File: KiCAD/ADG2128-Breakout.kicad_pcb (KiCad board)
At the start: 2 copper layers, 18.8 x 36.6 mm, 10 parts, among them J1 Conn_01x14_Male, J2 Conn_01x14_Male, J3 Conn_01x03_Male, J4 Conn_01x03_Male, J5 Conn_01x03_Male, U1 ADG2128

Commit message: Fixing silk mistake.
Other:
- board text added: "Vcc GND SDA SCL ~RESET GND Y0 Y1 Y2 Y3 Y4 Y5 Y6 Y7"
- board text removed: "Vcc GND SDA SCL ~RESET SDA Y0 Y1 Y2 Y3 Y4 Y5 Y6 Y7"
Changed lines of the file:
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@@
     (effects (font (size 1.5 1.5) (thickness 0.3)) (justify left mirror))
   )
-  (gr_text "Vcc\nGND\nSDA\nSCL\n~RESET\nSDA\nY0\nY1\nY2\nY3\nY4\nY5\nY6\nY7" (at 24.5745 34.417) (layer B.SilkS)
+  (gr_text "Vcc\nGND\nSDA\nSCL\n~RESET\nGND\nY0\nY1\nY2\nY3\nY4\nY5\nY6\nY7" (at 24.5745 34.417) (layer B.SilkS)
     (effects (font (size 1.5 1.5) (thickness 0.3)) (justify right mirror))
   )

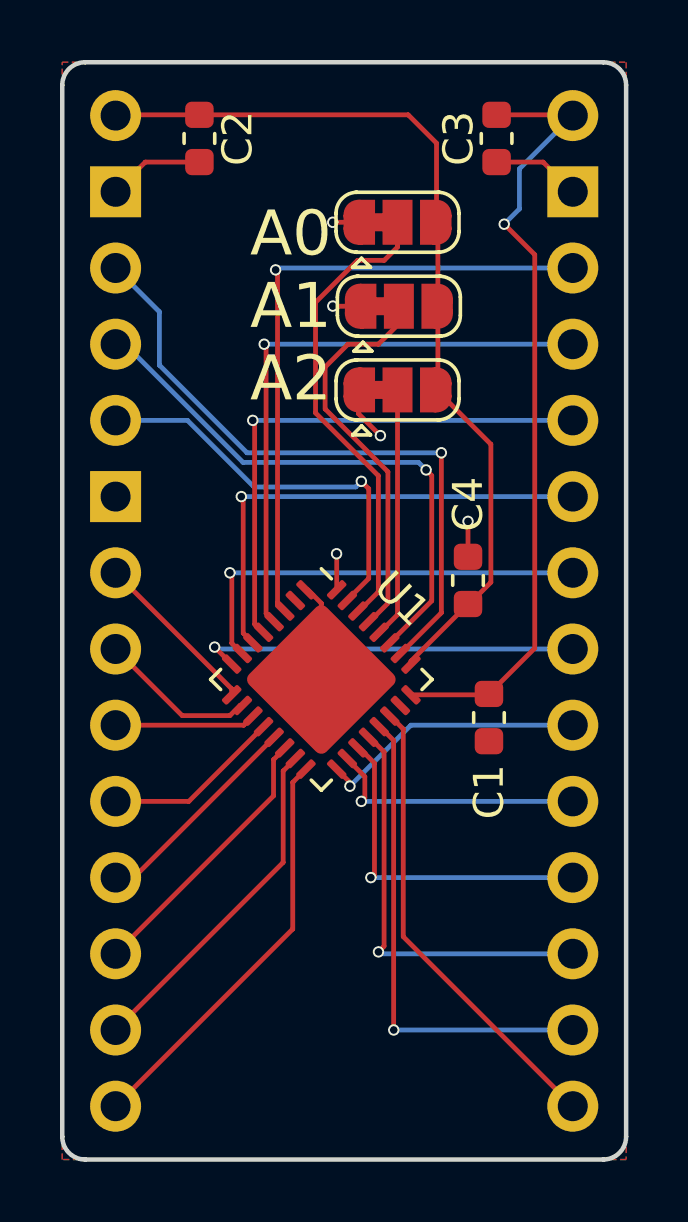
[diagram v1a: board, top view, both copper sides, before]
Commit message: Minor revisions for better manufacturability.
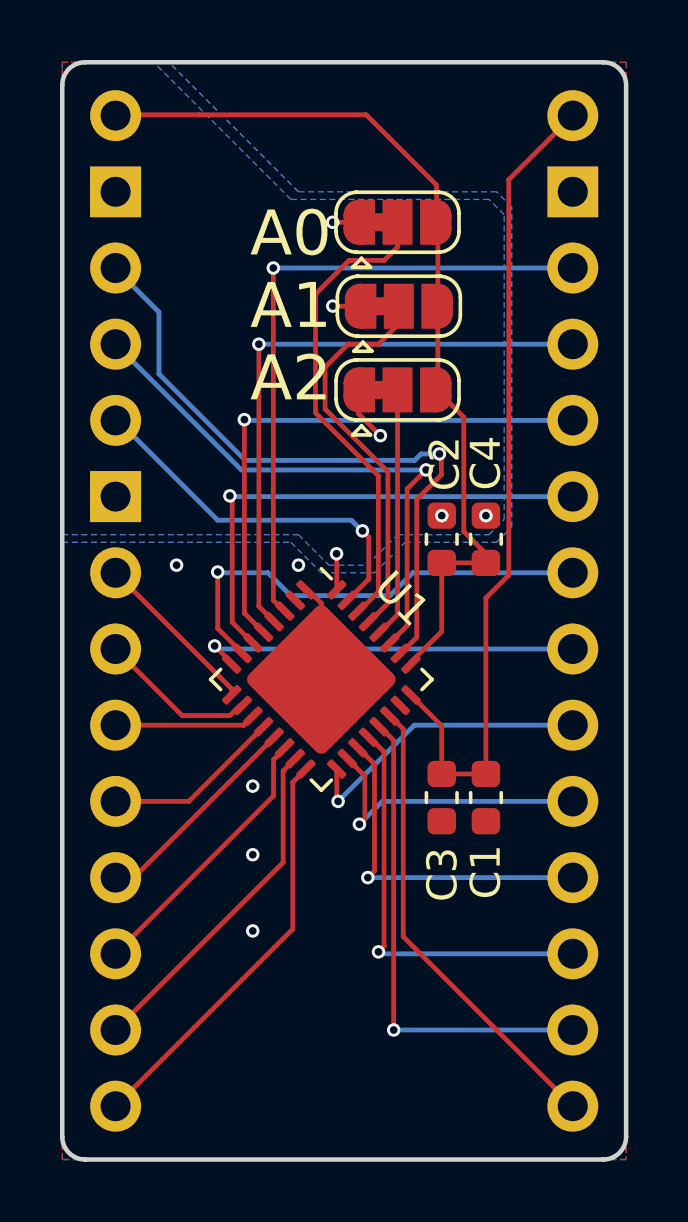
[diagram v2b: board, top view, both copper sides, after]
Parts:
- moved C3 22.0 mm to (33.7, 40.5)
- moved C2 15.6 mm to (33.7, 31.9), turned to 90 degrees
- moved C1 2.67 mm to (35.2, 40.5)
- moved C4 1.50 mm to (35.2, 31.9)
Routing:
- net /GND: track 9.18 -> 4.80 mm, vias 5 -> 6
- net /ANAGND: track 6.19 -> 3.24 mm, vias 0 -> 5
- net /ANAVcc: track 26.4 -> 27.7 mm, vias 1 -> 0
- net /X4: track 14.3 -> 15.5 mm
- net /X7: track 8.77 -> 9.94 mm
- net /~RESET: track 13.6 -> 12.6 mm
- net /X6: track 9.07 -> 9.97 mm
- net /X3: track 16.1 -> 16.7 mm
- added copper zone on B.Cu, net /ANAGND
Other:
- net class Default: via_dia 0.38 -> 0.45
